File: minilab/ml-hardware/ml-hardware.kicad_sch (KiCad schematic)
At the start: 21 parts, among them J1 Conn_01x08, J10 BE_Skt-10, J11 BE_Skt-10, J12 BE_Skt-10, J13 BE_Skt-10, J14 BE-Cnn-10, J15 BE-Cnn-10, J16 Molex lite-trap, J17 Molex lite-trap, J18 Molex lite-trap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

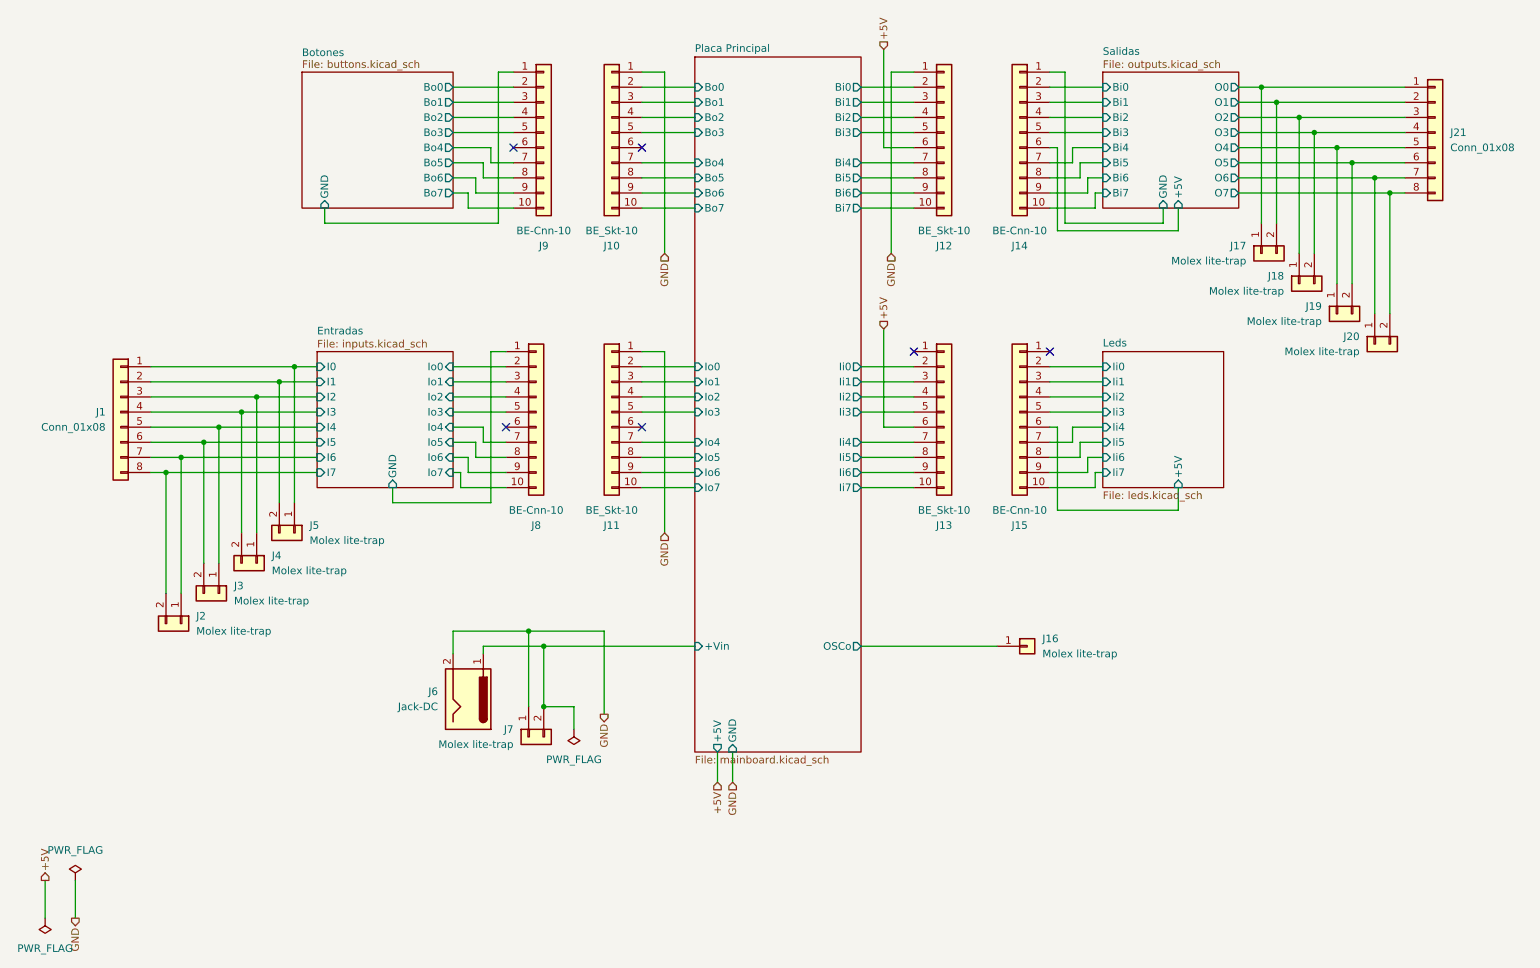
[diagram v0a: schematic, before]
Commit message: Dev minilab (#1)
* minilab: Add PCB (wip)

* minilab: Added fp and sym lib tables

* minilab: cambia jerarquia y agrega pcb

* minilab: Agrega 2da opc conectores y modelos 3d
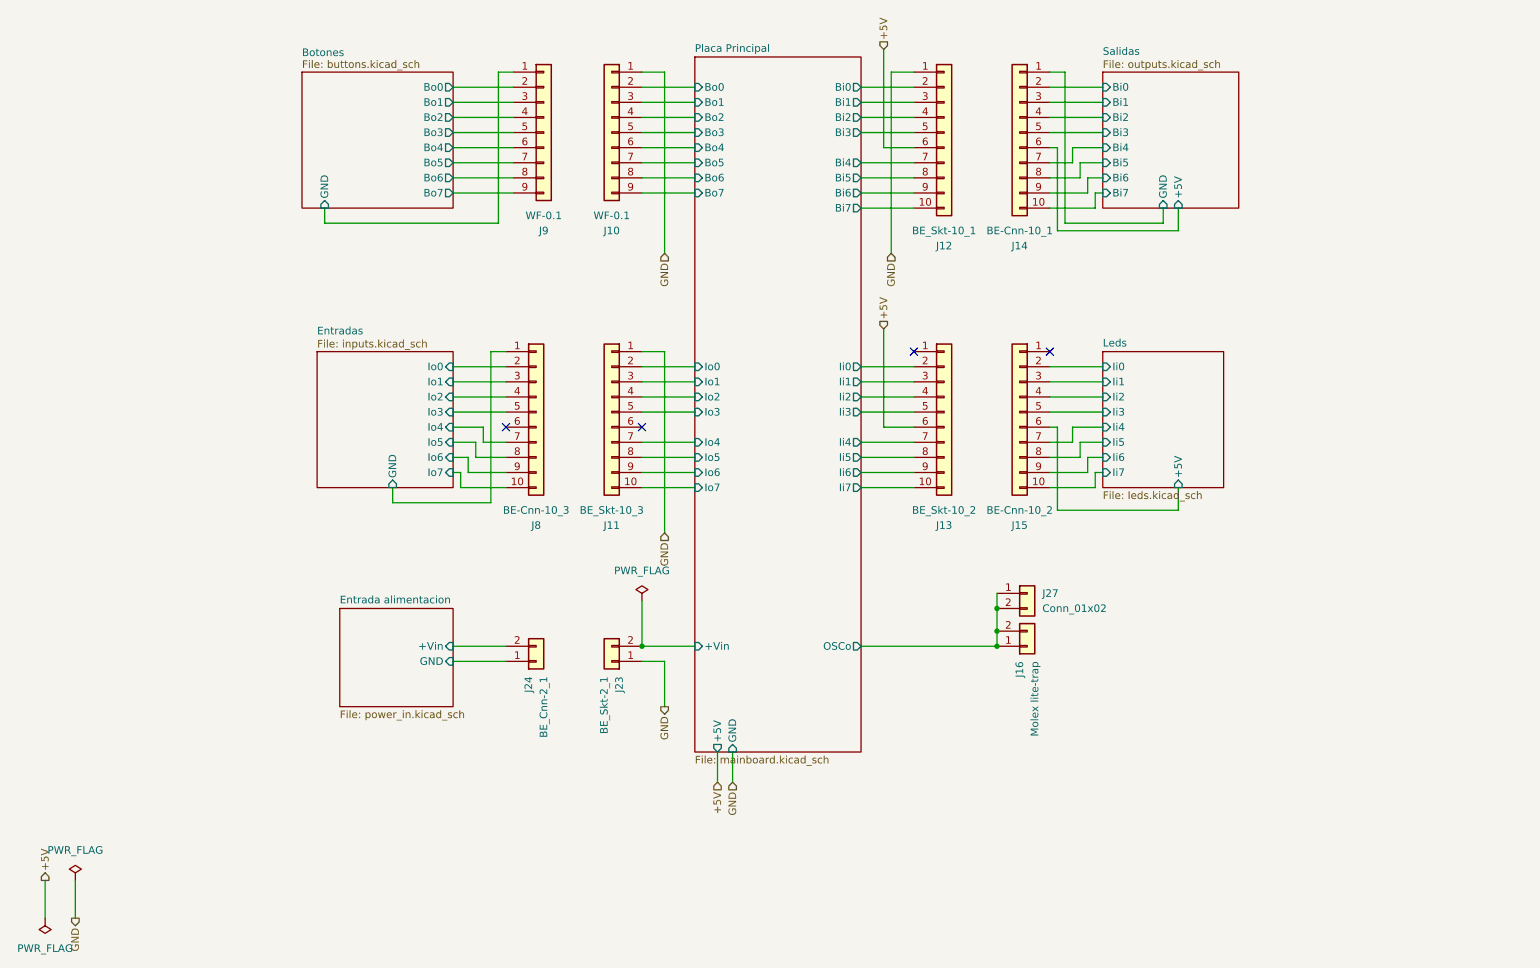
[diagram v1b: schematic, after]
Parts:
- removed J1, J21: Conn_01x08, Connector_PinSocket_2.54mm:PinSocket_1x08_P2.54mm_Horizontal, symbol Connector_Generic:Conn_01x08
- removed J16: Molex lite-trap, Extras:104238-0210, symbol Connector_Generic:Conn_01x01
- removed J17, J18, J19, J2, J20, J3, J4, J5, J7: Molex lite-trap, Extras:104238-0210, symbol Connector_Generic:Conn_01x02
- removed J6: Jack-DC, Connector_BarrelJack:BarrelJack_Horizontal, symbol Connector:Jack-DC
- added J16: Molex lite-trap, Extras:104238-0210, symbol Connector_Generic:Conn_01x02
- added J23: BE_Skt-2_1, Extras:EdgeSocket-2, symbol Connector_Generic:Conn_01x02
- added J24: BE_Cnn-2_1, Extras:EdgeConn-2, symbol Connector_Generic:Conn_01x02
- added J27: Conn_01x02, Connector_PinSocket_2.54mm:PinSocket_1x02_P2.54mm_Horizontal, symbol Connector_Generic:Conn_01x02
- J10: value BE_Skt-10 -> WF-0.1; footprint Extras:EdgeSocket-10 -> Connector_Molex:Molex_KK-254_AE-6410-09A_1x09_P2.54mm_Vertical; symbol Connector_Generic:Conn_01x10 -> Connector_Generic:Conn_01x09
- J11: value BE_Skt-10 -> BE_Skt-10_3
- J12: value BE_Skt-10 -> BE_Skt-10_1
- J13: value BE_Skt-10 -> BE_Skt-10_2
- J14: value BE-Cnn-10 -> BE-Cnn-10_1
- J15: value BE-Cnn-10 -> BE-Cnn-10_2
- J8: value BE-Cnn-10 -> BE-Cnn-10_3
- J9: value BE-Cnn-10 -> WF-0.1; footprint Extras:EdgeConn-10 -> Connector_Molex:Molex_KK-254_AE-6410-09A_1x09_P2.54mm_Vertical; symbol Connector_Generic:Conn_01x10 -> Connector_Generic:Conn_01x09
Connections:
- net Botones/Bo4: now also J9.6 (Pin_6); no longer J9.7 (Pin_7)
- net Botones/Bo5: now also J9.7 (Pin_7); no longer J9.8 (Pin_8)
- net Botones/Bo6: now also J9.8 (Pin_8); no longer J9.9 (Pin_9)
- net Botones/Bo7: now also J9.9 (Pin_9); no longer J9.10 (Pin_10)
- net GND: now also J23.1 (Pin_1)
- net Placa Principal/+Vin: now also J23.2 (Pin_2)
- net Placa Principal/Bo4: now also J10.6 (Pin_6); no longer J10.7 (Pin_7)
- net Placa Principal/Bo5: now also J10.7 (Pin_7); no longer J10.8 (Pin_8)
- net Placa Principal/Bo6: now also J10.8 (Pin_8); no longer J10.9 (Pin_9)
- net Placa Principal/Bo7: now also J10.9 (Pin_9); no longer J10.10 (Pin_10)
- net Placa Principal/OSCo: now also J16.1 (Pin_1), J16.2 (Pin_2), J27.1 (Pin_1), J27.2 (Pin_2)
- new net Entrada alimentacion/+Vin: J24.2 (Pin_2)
- new net Entrada alimentacion/GND: J24.1 (Pin_1)
- no-connect marks 6 -> 4
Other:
- added sheet Entrada alimentacion (power_in.kicad_sch)
- sheet Entradas ports: added none; removed I0, I1, I2, I3, I4, I5, I6, I7
- sheet Salidas ports: added none; removed O0, O1, O2, O3, O4, O5, O6, O7
